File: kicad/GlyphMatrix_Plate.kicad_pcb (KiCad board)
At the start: 2 copper layers, 294.9 x 128.6 mm, 0 parts

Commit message: added MCU
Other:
- board size 294.9 x 128.6 mm -> 295 x 128.6 mm
- board text added: "OminCode:9001 v0.3.1"

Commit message: updated MCU
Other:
- board text added: "OminCode:9001 v0.3.4"
- board text removed: "OminCode:9001 v0.3.1"
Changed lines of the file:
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@@
   (title_block
     (title "GlyphMatrix_Plate")
-    (date "2025-07-02")
-    (rev "0.3.3")
+    (date "2025-07-03")
+    (rev "0.3.4")
     (company "Allen Choi")
   )
@@
     )
   )
-  (gr_text "OminCode:9001 v0.3.1"
+  (gr_text "OminCode:9001 v0.3.4"
     (at 201.20625 190.0125 0)
     (layer "F.SilkS" knockout)

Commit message: screw holes
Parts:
- added H1: MountingHole_3.2mm_Pad, TB2086_MISC:MountingHole_3.2mm_Pad, F.Cu at (64.9, 79.7)
- added H2: MountingHole_3.2mm_Pad, TB2086_MISC:MountingHole_3.2mm_Pad, F.Cu at (351.8, 79.7)
- added H3: MountingHole_3.2mm_Pad, TB2086_MISC:MountingHole_3.2mm_Pad, F.Cu at (351.8, 200.3)
- added H4: MountingHole_3.2mm_Pad, TB2086_MISC:MountingHole_3.2mm_Pad, F.Cu at (64.9, 200.3)
- added H5: MountingHole_3.2mm_Pad, TB2086_MISC:MountingHole_3.2mm_Pad, F.Cu at (207.8, 79.7)
- added H6: MountingHole_3.2mm_Pad, TB2086_MISC:MountingHole_3.2mm_Pad, F.Cu at (214.7, 190.0)
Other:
- board size 295 x 128.6 mm -> 294.9 x 128.6 mm

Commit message: pogo pin - ergogen
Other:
- board size 294.9 x 128.6 mm -> 295 x 128.6 mm

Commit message: changed screw sizes
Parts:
- H1, H2, H3, H4, H5, H6: value MountingHole_3.2mm_Pad -> MountingHole_2.2mm_M2_Pad; footprint TB2086_MISC:MountingHole_3.2mm_Pad -> TB2086_MISC:MountingHole_2.2mm_M2_Pad
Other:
- board size 295 x 128.6 mm -> 298.4 x 128.6 mm
- board text added: "OminCode:9001 20250709"
- board text removed: "OminCode:9001 v0.3.4"

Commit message: fixed positions for screw holes
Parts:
- moved H2 1.41 mm to (350.8, 80.7)
- moved H3 1.41 mm to (350.8, 199.3)
- moved H1 1.41 mm to (65.9, 80.7)
- moved H4 1.41 mm to (65.9, 199.3)
- moved H5 1.41 mm to (208.8, 80.7)
- moved H6 1.00 mm to (215.7, 190.0)
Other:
- board size 298.4 x 128.6 mm -> 298.3 x 128.6 mm

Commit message: more tweaks  (#3)
* small tweaks

* GlyphMatrix - 3mm screws

* PhaseShift - 3mm screws

* DeltaForm - 3mm screws

* updated README.md
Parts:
- H1, H2, H3, H4, H5, H6: value MountingHole_2.2mm_M2_Pad -> MountingHole_3.2mm_Pad; footprint TB2086_MISC:MountingHole_2.2mm_M2_Pad -> TB2086_MISC:MountingHole_3.2mm_Pad
- moved H1 0.71 mm to (65.4, 80.2)
- moved H2 0.71 mm to (351.3, 80.2)
- moved H3 0.71 mm to (351.3, 199.8)
- moved H4 0.71 mm to (65.4, 199.8)
- moved H5 0.64 mm to (208.3, 80.2)
- moved H6 0.50 mm to (215.2, 190.0)
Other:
- board text added: "OminCode:9001 202507.12"
- board text removed: "OminCode:9001 20250709"
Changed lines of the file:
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@@
 	(title_block
 		(title "GlyphMatrix_Plate")
-		(date "2025-07-09")
-		(rev "0.4.3")
+		(date "2025-07-11")
+		(rev "0.4.9")
 		(company "Allen Choi")
 	)
@@
 	(net 0 "")
 	(net 1 "GND")
-	(footprint "TB2086_MISC:MountingHole_2.2mm_M2_Pad"
+	(footprint "TB2086_MISC:MountingHole_3.2mm_Pad"
 		(layer "F.Cu")
-		(at 208.75 80.7125)
-		(descr "Mounting Hole 2.2mm, M2")
-		(tags "mounting hole 2.2mm m2")
+		(at 208.35 80.2125)
+		(descr "Mounting Hole 3.2mm, no annular, M3")
+		(tags "mounting hole 3.2mm no annular m3")
 		(property "Reference" "H5"
-			(at 0 -3.2 0)
+			(at 0 -4.2 0)
 			(layer "F.SilkS")
 			(hide yes)
@@
 			)
 		)
-		(property "Value" "MountingHole_2.2mm_M2_Pad"
-			(at 0 3.2 0)
+		(property "Value" "MountingHole_3.2mm_Pad"
+			(at 0 4.2 0)
 			(layer "F.Fab")
 			(effects
@@
 		(fp_circle
 			(center 0 0)
-			(end 2.2 0)
+			(end 3.2 0)
 			(stroke
 				(width 0.15)
@@
 		(fp_circle
 			(center 0 0)
-			(end 2.45 0)
+			(end 3.45 0)
 			(stroke
 				(width 0.05)
@@
 		(pad "1" thru_hole circle
 			(at 0 0)
-			(size 4.4 4.4)
-			(drill 2.2)
+			(size 3.5 3.5)
+			(drill 3.2)
 			(layers "*.Cu" "*.Mask")
 			(remove_unused_layers no)
 			(net 1 "GND")
+			(zone_connect 2)
 		)
 		(embedded_fonts no)
 	)
-	(footprint "TB2086_MISC:MountingHole_2.2mm_M2_Pad"
+	(footprint "TB2086_MISC:MountingHole_3.2mm_Pad"
 		(layer "F.Cu")
-		(at 350.825 80.7125)
-		(descr "Mounting Hole 2.2mm, M2")
-		(tags "mounting hole 2.2mm m2")
-		(property "Reference" "H2"
-			(at 0 -3.2 0)
+		(at 215.23125 190.0125)
+		(descr "Mounting Hole 3.2mm, no annular, M3")
+		(tags "mounting hole 3.2mm no annular m3")
+		(property "Reference" "H6"
+			(at 0 -4.2 0)
 			(layer "F.SilkS")
 			(hide yes)
@@
 			)
 		)
-		(property "Value" "MountingHole_2.2mm_M2_Pad"
-			(at 0 3.2 0)
+		(property "Value" "MountingHole_3.2mm_Pad"
+			(at 0 4.2 0)
 			(layer "F.Fab")
 			(effects
@@
 		(fp_circle
 			(center 0 0)
-			(end 2.2 0)
+			(end 3.2 0)
 			(stroke
 				(width 0.15)
@@
 		(fp_circle
 			(center 0 0)
-			(end 2.45 0)
+			(end 3.45 0)
 			(stroke
 				(width 0.05)
@@
 		(pad "1" thru_hole circle
 			(at 0 0)
-			(size 4.4 4.4)
-			(drill 2.2)
+			(size 3.5 3.5)
+			(drill 3.2)
 			(layers "*.Cu" "*.Mask")
 			(remove_unused_layers no)
 			(net 1 "GND")
+			(zone_connect 2)
 		)
 		(embedded_fonts no)
 	)
-	(footprint "TB2086_MISC:MountingHole_2.2mm_M2_Pad"
+	(footprint "TB2086_MISC:MountingHole_3.2mm_Pad"
 		(layer "F.Cu")
-		(at 350.825 199.3)
-		(descr "Mounting Hole 2.2mm, M2")
-		(tags "mounting hole 2.2mm m2")
+		(at 351.325 199.8)
+		(descr "Mounting Hole 3.2mm, no annular, M3")
+		(tags "mounting hole 3.2mm no annular m3")
 		(property "Reference" "H3"
-			(at 0 -3.2 0)
+			(at 0 -4.2 0)
 			(layer "F.SilkS")
 			(hide yes)
@@
 			)
 		)
-		(property "Value" "MountingHole_2.2mm_M2_Pad"
-			(at 0 3.2 0)
+		(property "Value" "MountingHole_3.2mm_Pad"
+			(at 0 4.2 0)
 			(layer "F.Fab")
 			(effects
@@
 		(fp_circle
 			(center 0 0)
-			(end 2.2 0)
+			(end 3.2 0)
 			(stroke
 				(width 0.15)
@@
 		(fp_circle
 			(center 0 0)
-			(end 2.45 0)
+			(end 3.45 0)
 			(stroke
 				(width 0.05)
@@
 		(pad "1" thru_hole circle
 			(at 0 0)
-			(size 4.4 4.4)
-			(drill 2.2)
+			(size 3.5 3.5)
+			(drill 3.2)
 			(layers "*.Cu" "*.Mask")
 			(remove_unused_layers no)
 			(net 1 "GND")
+			(zone_connect 2)
 		)
 		(embedded_fonts no)
 	)
-	(footprint "TB2086_MISC:MountingHole_2.2mm_M2_Pad"
+	(footprint "TB2086_MISC:MountingHole_3.2mm_Pad"
 		(layer "F.Cu")
-		(at 215.73125 190.0125)
-		(descr "Mounting Hole 2.2mm, M2")
-		(tags "mounting hole 2.2mm m2")
-		(property "Reference" "H6"
-			(at 0 -3.2 0)
+		(at 65.375 199.8)
+		(descr "Mounting Hole 3.2mm, no annular, M3")
+		(tags "mounting hole 3.2mm no annular m3")
+		(property "Reference" "H4"
+			(at 0 -4.2 0)
 			(layer "F.SilkS")
 			(hide yes)
@@
 			)
 		)
-		(property "Value" "MountingHole_2.2mm_M2_Pad"
-			(at 0 3.2 0)
+		(property "Value" "MountingHole_3.2mm_Pad"
+			(at 0 4.2 0)
 			(layer "F.Fab")
 			(effects
@@
 		(fp_circle
 			(center 0 0)
-			(end 2.2 0)
+			(end 3.2 0)
 			(stroke
 				(width 0.15)
@@
 		(fp_circle
 			(center 0 0)
-			(end 2.45 0)
+			(end 3.45 0)
 			(stroke
 				(width 0.05)
@@
 		(pad "1" thru_hole circle
 			(at 0 0)
-			(size 4.4 4.4)
-			(drill 2.2)
+			(size 3.5 3.5)
+			(drill 3.2)
 			(layers "*.Cu" "*.Mask")
 			(remove_unused_layers no)
 			(net 1 "GND")
+			(zone_connect 2)
 		)
 		(embedded_fonts no)
 	)
-	(footprint "TB2086_MISC:MountingHole_2.2mm_M2_Pad"
+	(footprint "TB2086_MISC:MountingHole_3.2mm_Pad"
 		(layer "F.Cu")
-		(at 65.875 80.7125)
-		(descr "Mounting Hole 2.2mm, M2")
-		(tags "mounting hole 2.2mm m2")
+		(at 65.375 80.2125)
+		(descr "Mounting Hole 3.2mm, no annular, M3")
+		(tags "mounting hole 3.2mm no annular m3")
 		(property "Reference" "H1"
-			(at 0 -3.2 0)
+			(at 0 -4.2 0)
 			(layer "F.SilkS")
 			(hide yes)
@@
 			)
 		)
-		(property "Value" "MountingHole_2.2mm_M2_Pad"
-			(at 0 3.2 0)
+		(property "Value" "MountingHole_3.2mm_Pad"
+			(at 0 4.2 0)
 			(layer "F.Fab")
 			(effects
@@
 		(fp_circle
 			(center 0 0)
-			(end 2.2 0)
+			(end 3.2 0)
 			(stroke
 				(width 0.15)
@@
 		(fp_circle
 			(center 0 0)
-			(end 2.45 0)
+			(end 3.45 0)
 			(stroke
 				(width 0.05)
@@
 		(pad "1" thru_hole circle
 			(at 0 0)
-			(size 4.4 4.4)
-			(drill 2.2)
+			(size 3.5 3.5)
+			(drill 3.2)
 			(layers "*.Cu" "*.Mask")
 			(remove_unused_layers no)
 			(net 1 "GND")
+			(zone_connect 2)
 		)
 		(embedded_fonts no)
 	)
-	(footprint "TB2086_MISC:MountingHole_2.2mm_M2_Pad"
+	(footprint "TB2086_MISC:MountingHole_3.2mm_Pad"
 		(layer "F.Cu")
-		(at 65.875 199.3)
-		(descr "Mounting Hole 2.2mm, M2")
-		(tags "mounting hole 2.2mm m2")
-		(property "Reference" "H4"
-			(at 0 -3.2 0)
+		(at 351.325 80.2125)
+		(descr "Mounting Hole 3.2mm, no annular, M3")
+		(tags "mounting hole 3.2mm no annular m3")
+		(property "Reference" "H2"
+			(at 0 -4.2 0)
 			(layer "F.SilkS")
 			(hide yes)
@@
 			)
 		)
-		(property "Value" "MountingHole_2.2mm_M2_Pad"
-			(at 0 3.2 0)
+		(property "Value" "MountingHole_3.2mm_Pad"
+			(at 0 4.2 0)
 			(layer "F.Fab")
 			(effects
@@
 		(fp_circle
 			(center 0 0)
-			(end 2.2 0)
+			(end 3.2 0)
 			(stroke
 				(width 0.15)
@@
 		(fp_circle
 			(center 0 0)
-			(end 2.45 0)
+			(end 3.45 0)
 			(stroke
 				(width 0.05)
@@
 		(pad "1" thru_hole circle
 			(at 0 0)
-			(size 4.4 4.4)
-			(drill 2.2)
+			(size 3.5 3.5)
+			(drill 3.2)
 			(layers "*.Cu" "*.Mask")
 			(remove_unused_layers no)
 			(net 1 "GND")
+			(zone_connect 2)
 		)
 		(embedded_fonts no)
@@
 	)
 	(gr_line
+		(start 61.175 75.7125)
+		(end 355.525 75.7125)
+		(stroke
+			(width 0.15)
+			(type default)
+		)
+		(layer "Edge.Cuts")
+	)
+	(gr_line
 		(start 357.525 77.7125)
 		(end 357.525 202.3)
@@
 		(layer "Edge.Cuts")
 	)
-	(gr_line
-		(start 355.525 204.3)
-		(end 61.175 204.3)
+	(gr_arc
+		(start 59.175 77.7125)
+		(mid 59.760786 76.298286)
+		(end 61.175 75.7125)
 		(stroke
 			(width 0.15)
@@
 	)
 	(gr_line
-		(start 61.175 75.7125)
-		(end 355.525 75.7125)
-		(stroke
-			(width 0.15)
-			(type default)
-		)
-		(layer "Edge.Cuts")
-	)
-	(gr_arc
-		(start 59.175 77.7125)
-		(mid 59.760786 76.298286)
-		(end 61.175 75.7125)
-		(stroke
-			(width 0.15)
-			(type default)
-		)
-		(layer "Edge.Cuts")
-	)
-	(gr_line
 		(start 59.175 202.3)
 		(end 59.175 77.7125)
@@
 		(layer "Edge.Cuts")
 	)
-	(gr_text "OminCode:9001 20250709"
-		(at 201.20625 190.0125 0)
+	(gr_line
+		(start 355.525 204.3)
+		(end 61.175 204.3)
+		(stroke
+			(width 0.15)
+			(type default)
+		)
+		(layer "Edge.Cuts")
+	)
+	(gr_text "OminCode:9001 202507.12"
+		(at 215.23125 185.0125 0)
 		(layer "F.SilkS" knockout)
 		(effects
 			(font
-				(face "KiCad Font")
 				(size 1.2 1.2)
 				(thickness 0.15)

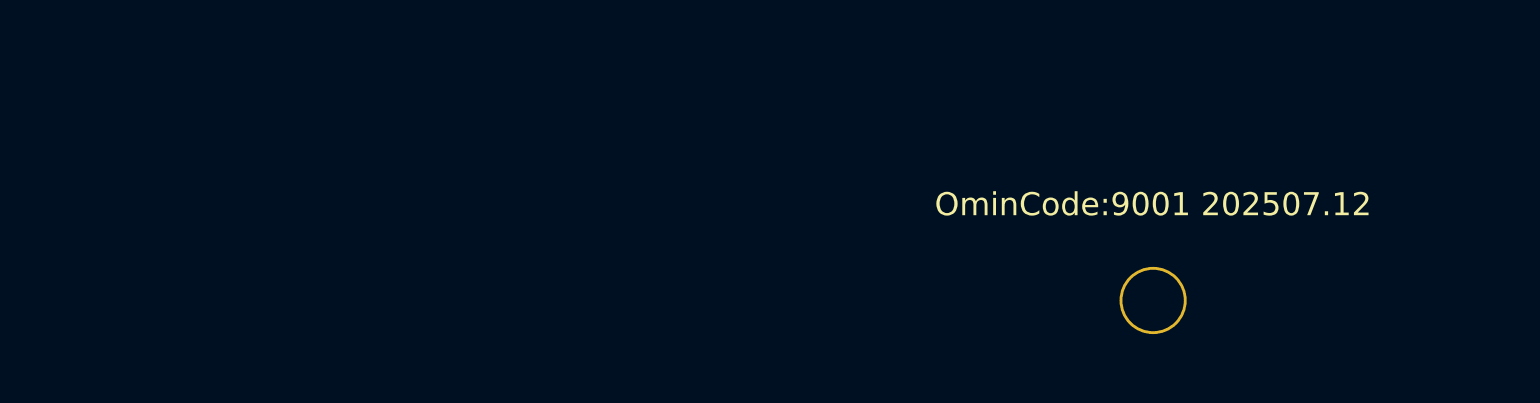
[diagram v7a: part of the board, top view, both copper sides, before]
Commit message: plates (#4)
* Silk Screen

* small changes for GlyphMatrix

* Silk screen for plates

* amended GlyphMatrix
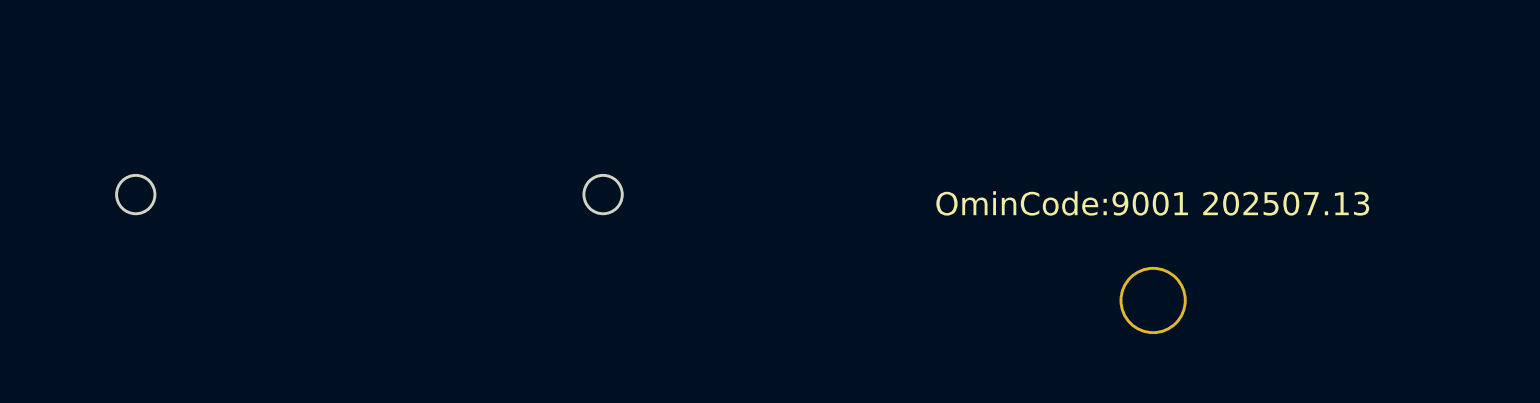
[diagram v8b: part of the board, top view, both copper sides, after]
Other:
- outline, holes or cut-outs redrawn
- board text added: "OminCode:9001 202507.13"
- board text added: "OmniCode:9001-GlyphMatrix"
- board text added: "RESET"
- board text added: "UPDATE"
- board text removed: "OminCode:9001 202507.12"
